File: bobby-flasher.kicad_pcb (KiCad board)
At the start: 2 copper layers, 17.4 x 29.4 mm, 28 parts, among them J1 Conn_01x03, J2 Conn_01x06, J3 Flash, Q1 SS8050_C2150, Q2 SS8050_C2150, U1 CH343G, U2 AMS1117-3.3

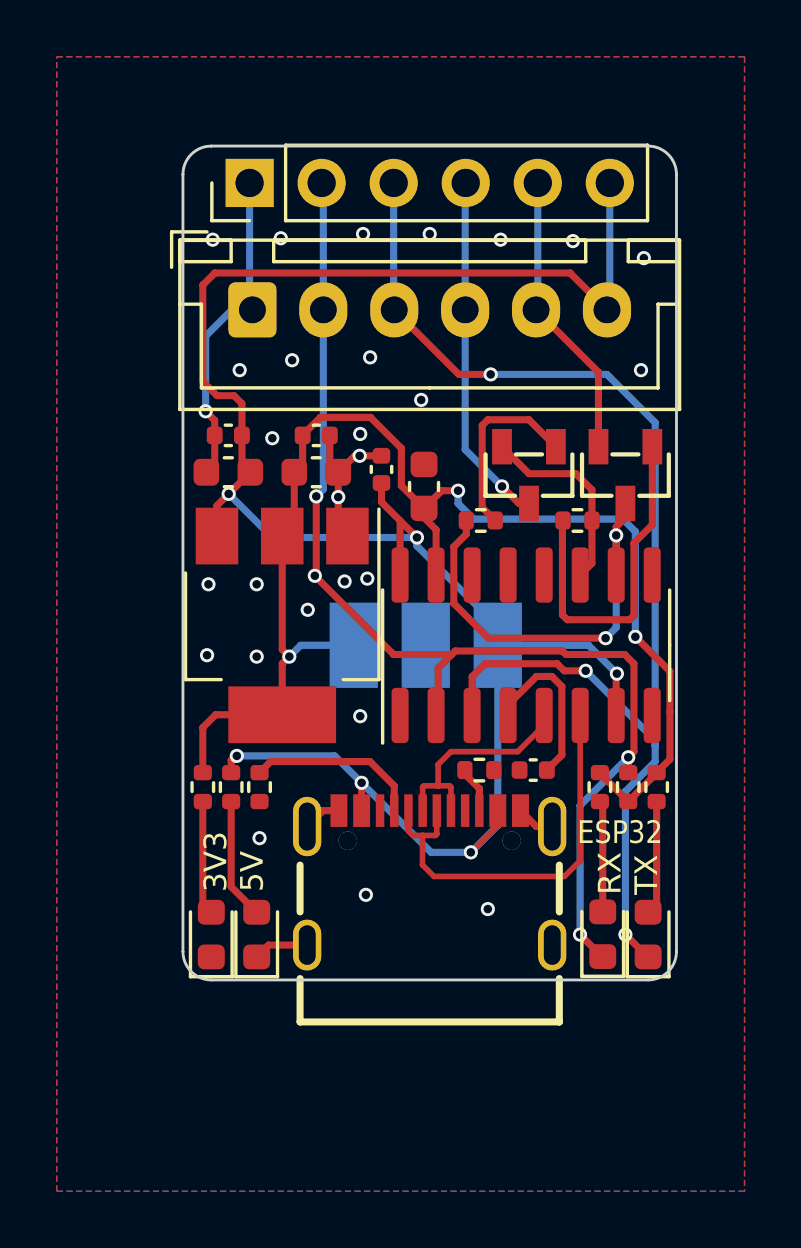
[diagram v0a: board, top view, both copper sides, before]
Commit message: Added 10k pullup to DTR
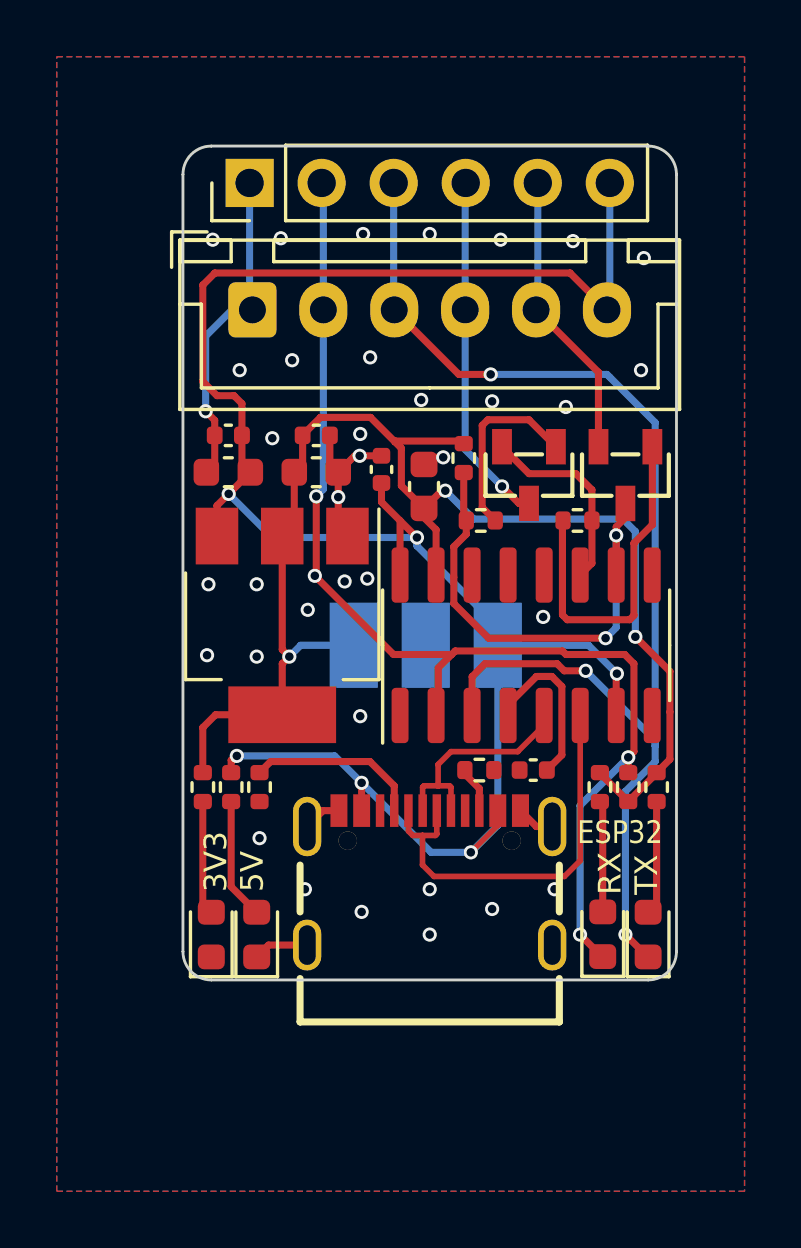
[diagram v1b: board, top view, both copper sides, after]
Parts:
- added R10: 10k, Resistor_SMD:R_0402_1005Metric, F.Cu at (1.20, 62.6)
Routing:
- net +3V3: track 47.2 -> 49.4 mm
- net DTR: track 15.4 -> 17.1 mm
- net GND: track 21.8 -> 22.6 mm, vias 28 -> 36
